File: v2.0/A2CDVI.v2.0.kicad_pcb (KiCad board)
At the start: 2 copper layers, 53.4 x 62.5 mm, 30 parts, among them J1 DA15_Plug, J2 Aux, SW1 Config, U1 RPI-Pico, U2 L7805, U3 74LVC245

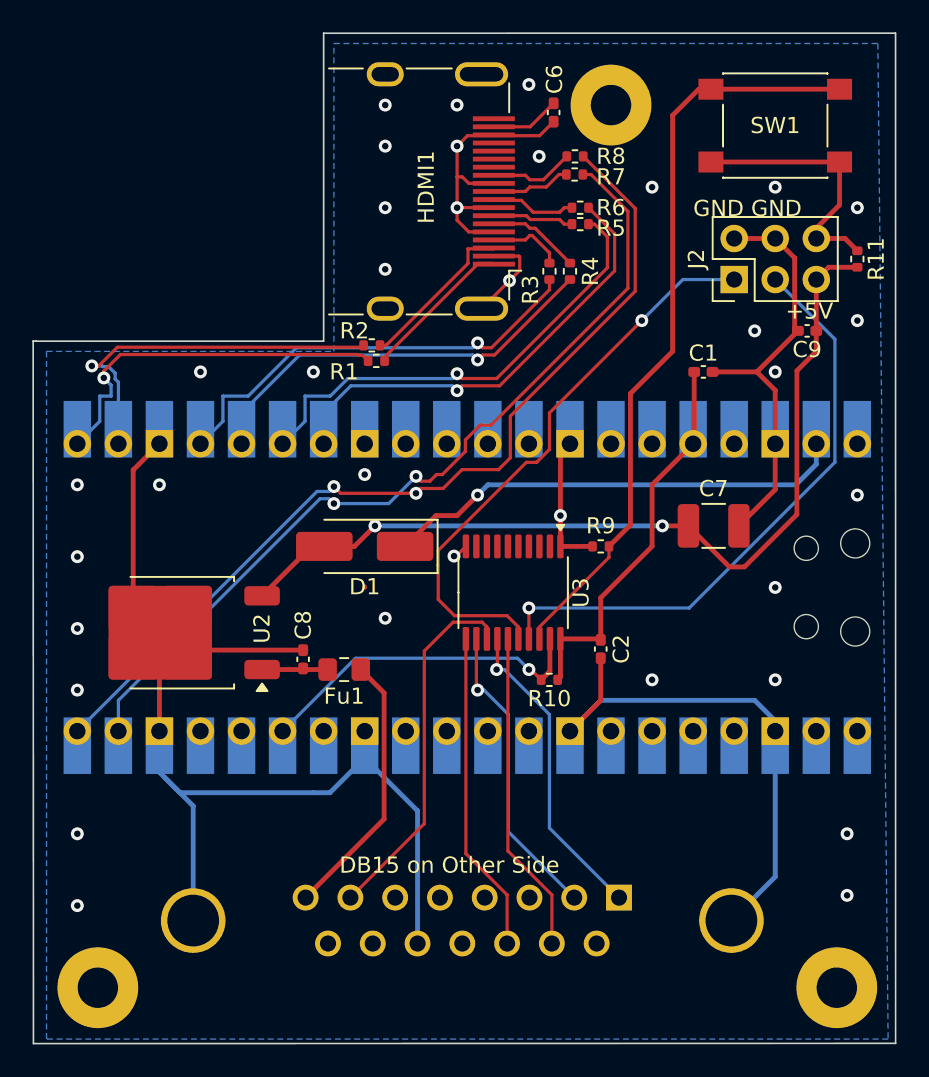
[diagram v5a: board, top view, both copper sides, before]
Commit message: Fixed DRC issues
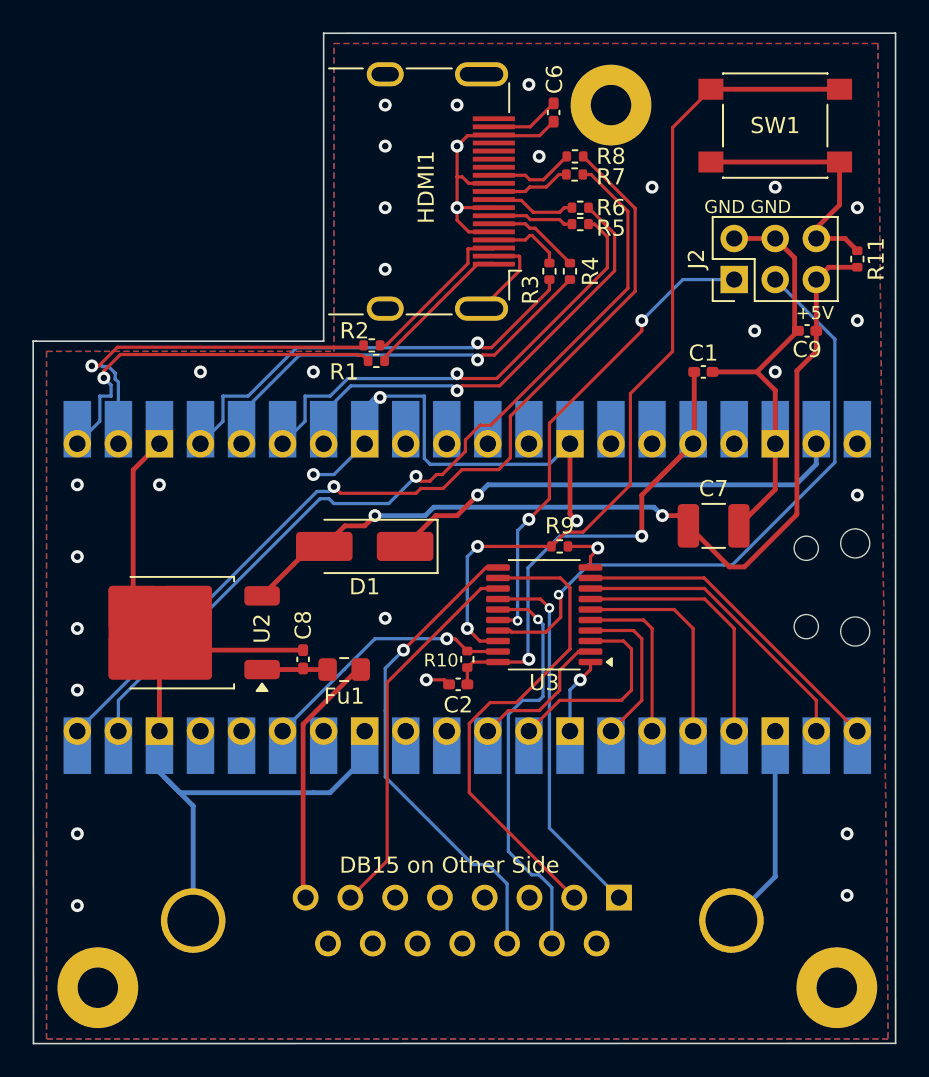
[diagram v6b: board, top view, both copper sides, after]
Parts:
- moved C2 9.09 mm to (127.6, 131.5), turned to 180 degrees
- moved R10 5.24 mm to (128.1, 129.9), turned to 90 degrees
- moved R9 2.54 mm to (133.9, 122.9), turned to 0 degrees
- moved U3 2.36 mm to (132.9, 127.2), turned to 180 degrees
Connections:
- HDMI1 pad GND: (no net) -> GND
- J1 pad 0: (no net) -> GND
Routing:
- net Net-(U1-GP0): track 0.00 -> 20.4 mm
- net Net-(U1-GP1): track 0.00 -> 18.7 mm
- net Net-(U1-GP2): track 0.00 -> 16.0 mm
- net Net-(U1-GP3): track 0.00 -> 13.2 mm
- net Net-(U1-GP6): track 0.00 -> 12.7 mm
- net Net-(J1-14M): track 18.7 -> 30.1 mm, vias 1 -> 0
- net +3V3: track 24.1 -> 34.6 mm, vias 0 -> 2
- net Net-(U1-GP4): track 0.00 -> 10.4 mm
- net Net-(J1-SEROUT): track 19.9 -> 30.2 mm, vias 0 -> 1
- net Net-(U1-GP5): track 0.00 -> 9.89 mm
- net Net-(U1-GP7): track 0.00 -> 9.74 mm
- net Net-(U3-B0): track 46.8 -> 53.1 mm, vias 0 -> 2
- net Net-(J2-Pin_1): track 36.0 -> 29.8 mm, vias 1 -> 3
- net Net-(J1-GR): track 20.0 -> 25.8 mm, vias 0 -> 1
- net Net-(U1-GP11): track 21.2 -> 16.0 mm
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- added copper zone on F.Cu, net GND
